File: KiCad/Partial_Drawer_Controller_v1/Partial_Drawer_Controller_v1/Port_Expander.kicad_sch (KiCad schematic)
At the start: 3 parts, among them U5 PCA9554PW,118

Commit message: feat: finishing first draft for `partial_drawer_controller_v1` schematic
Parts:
- removed C52: 100n_50V, Capacitor_SMD:C_0402_1005Metric, symbol _C_0402:100n_50V
- removed R220: 10K, Resistor_SMD:R_0402_1005Metric, symbol _R_0402:10K
- removed U5: PCA9554PW,118, Package_SO:TSSOP-16_4.4x5mm_P0.65mm, symbol _Interface_Expansion:PCA9554PW,118
- added C72: 100n_50V, Capacitor_SMD:C_0402_1005Metric, symbol _C_0402:100n_50V
- added R241: 10K, Resistor_SMD:R_0402_1005Metric, symbol _R_0402:10K
- added U5: PCA9535PW,118, Package_SO:TSSOP-24_4.4x7.8mm_P0.65mm, symbol _Interface_Expansion:PCA9535PW,118
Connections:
- net +5V: now also C72.1, R241.1, U5.24 (VDD)
- net A0: now also U5.21 (A0)
- net A1: now also U5.2 (A1)
- net A2: now also U5.3 (A2)
- net GND: now also C72.2, U5.12 (VSS)
- net SCL: now also U5.23 (SDA)
- net SDA: now also U5.22 (SCL)
- net ~INT: now also R241.2, U5.1 (~INT)
- new net IO0_0: U5.4 (IO0_0)
- new net IO0_1: U5.5 (IO0_1)
- new net IO0_2: U5.6 (IO0_2)
- new net IO0_3: U5.7 (IO0_3)
- new net IO0_4: U5.8 (IO0_4)
- new net IO0_5: U5.9 (IO0_5)
- new net IO0_6: U5.10 (IO0_6)
- new net IO0_7: U5.11 (IO0_7)
- new net IO1_0: U5.13 (IO1_0)
- new net IO1_1: U5.14 (IO1_1)
- new net IO1_2: U5.15 (IO1_2)
- new net IO1_3: U5.16 (IO1_3)
- new net IO1_4: U5.17 (IO1_4)
- new net IO1_5: U5.18 (IO1_5)
- new net IO1_6: U5.19 (IO1_6)
- new net IO1_7: U5.20 (IO1_7)

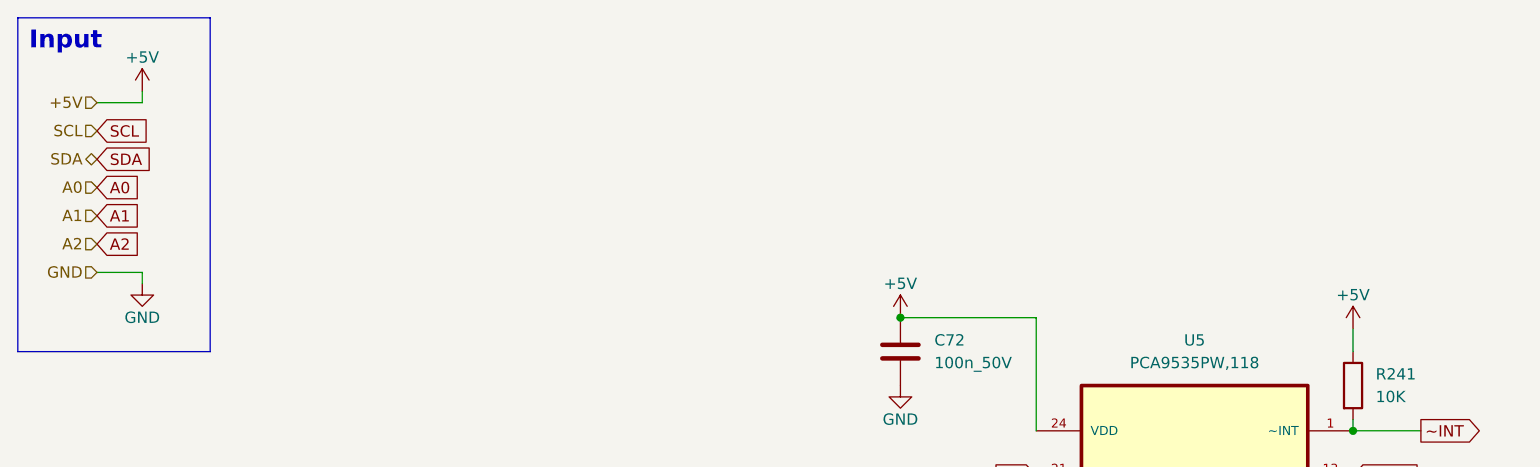
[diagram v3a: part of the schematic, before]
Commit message: feat: routing almost done - design rule check still missing
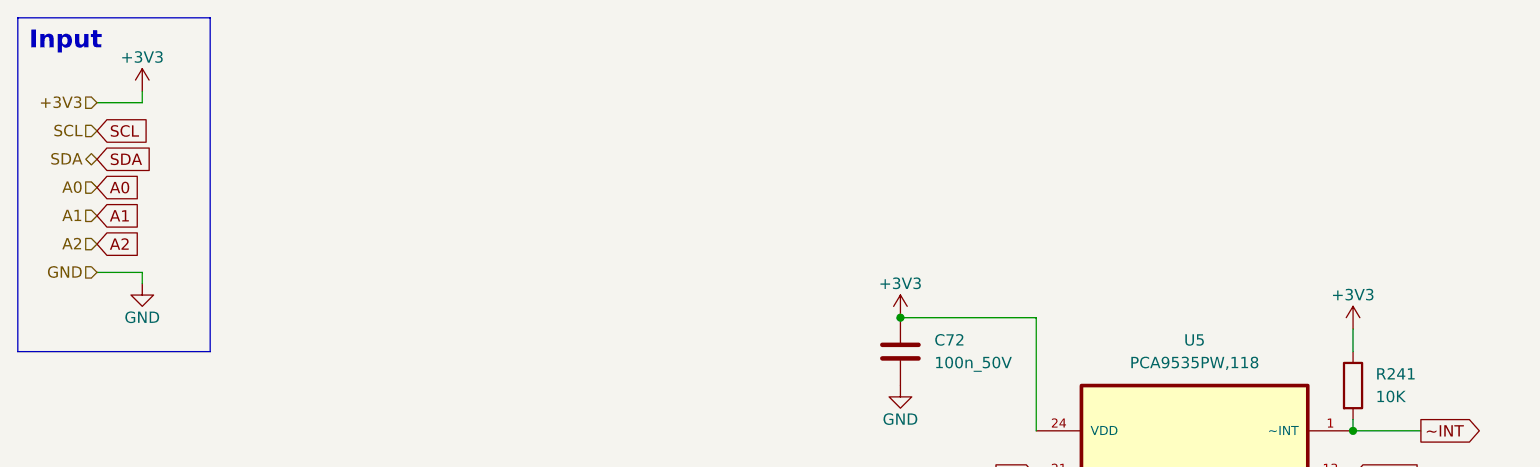
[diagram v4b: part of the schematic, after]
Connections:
- net +5V renamed +3V3
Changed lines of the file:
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@@
 		)
 	)
-	(hierarchical_label "+5V"
+	(hierarchical_label "+3V3"
 		(shape input)
 		(at 24.13 25.4 180)
@@
 			)
 			(justify left)
+		)
+	)
+	(symbol
+		(lib_id "power:+3V3")
+		(at 114.3 49.53 0)
+		(unit 1)
+		(exclude_from_sim no)
+		(in_bom yes)
+		(on_board yes)
+		(dnp no)
+		(property "Reference" "#PWR0192"
+			(at 114.3 53.34 0)
+			(effects
+				(font
+					(size 1.27 1.27)
+				)
+				(hide yes)
+			)
+		)
+		(property "Value" "+3V3"
+			(at 114.3 45.72 0)
+			(effects
+				(font
+					(size 1.27 1.27)
+				)
+			)
+		)
+		(property "Footprint" ""
+			(at 114.3 49.53 0)
+			(effects
+				(font
+					(size 1.27 1.27)
+				)
+				(hide yes)
+			)
+		)
+		(property "Datasheet" ""
+			(at 114.3 49.53 0)
+			(effects
+				(font
+					(size 1.27 1.27)
+				)
+				(hide yes)
+			)
+		)
+		(property "Description" ""
+			(at 114.3 49.53 0)
+			(effects
+				(font
+					(size 1.27 1.27)
+				)
+				(hide yes)
+			)
+		)
+		(pin "1"
+		)
+		(instances
+			(project "Partial_Drawer_Controller_v1"
+				(path "/57f8c193-fe09-43d3-9441-dbd40881d2aa/d19b84cd-4ee4-4d95-811d-38c072072447/1435e788-24b0-4d35-b04b-da1d0e65b7d1"
+					(reference "#PWR0192")
+					(unit 1)
+				)
+				(path "/57f8c193-fe09-43d3-9441-dbd40881d2aa/d19b84cd-4ee4-4d95-811d-38c072072447/336007e7-e816-41c4-9905-48078505cd87"
+					(reference "#PWR0196")
+					(unit 1)
+				)
+				(path "/57f8c193-fe09-43d3-9441-dbd40881d2aa/d19b84cd-4ee4-4d95-811d-38c072072447/784b2884-d726-456d-9cf9-7365a865d845"
+					(reference "#PWR0200")
+					(unit 1)
+				)
+			)
 		)
 	)
@@
 	)
 	(symbol
-		(lib_id "power:+5V")
-		(at 165.1 50.8 0)
-		(unit 1)
-		(exclude_from_sim no)
-		(in_bom yes)
-		(on_board yes)
-		(dnp no)
-		(property "Reference" "#PWR0300"
-			(at 165.1 54.61 0)
-			(effects
-				(font
-					(size 1.27 1.27)
-				)
-				(hide yes)
-			)
-		)
-		(property "Value" "+5V"
-			(at 165.1 46.99 0)
-			(effects
-				(font
-					(size 1.27 1.27)
-				)
-			)
-		)
-		(property "Footprint" ""
-			(at 165.1 50.8 0)
-			(effects
-				(font
-					(size 1.27 1.27)
-				)
-				(hide yes)
-			)
-		)
-		(property "Datasheet" ""
-			(at 165.1 50.8 0)
-			(effects
-				(font
-					(size 1.27 1.27)
-				)
-				(hide yes)
-			)
-		)
-		(property "Description" ""
-			(at 165.1 50.8 0)
-			(effects
-				(font
-					(size 1.27 1.27)
-				)
-				(hide yes)
-			)
-		)
-		(pin "1"
-		)
-		(instances
-			(project "Partial_Drawer_Controller_v1"
-				(path "/57f8c193-fe09-43d3-9441-dbd40881d2aa/d19b84cd-4ee4-4d95-811d-38c072072447/784b2884-d726-456d-9cf9-7365a865d845"
-					(reference "#PWR0300")
-					(unit 1)
-				)
-				(path "/57f8c193-fe09-43d3-9441-dbd40881d2aa/d19b84cd-4ee4-4d95-811d-38c072072447/1435e788-24b0-4d35-b04b-da1d0e65b7d1"
-					(reference "#PWR0195")
-					(unit 1)
-				)
-				(path "/57f8c193-fe09-43d3-9441-dbd40881d2aa/d19b84cd-4ee4-4d95-811d-38c072072447/336007e7-e816-41c4-9905-48078505cd87"
-					(reference "#PWR0203")
-					(unit 1)
-				)
-			)
-		)
-	)
-	(symbol
 		(lib_id "_C_0402:100n_50V")
 		(at 114.3 53.34 0)
@@
 				(path "/57f8c193-fe09-43d3-9441-dbd40881d2aa/d19b84cd-4ee4-4d95-811d-38c072072447/336007e7-e816-41c4-9905-48078505cd87"
 					(reference "C53")
-					(unit 1)
-				)
-			)
-		)
-	)
-	(symbol
-		(lib_id "power:+5V")
-		(at 29.21 24.13 0)
-		(unit 1)
-		(exclude_from_sim no)
-		(in_bom yes)
-		(on_board yes)
-		(dnp no)
-		(property "Reference" "#PWR0182"
-			(at 29.21 27.94 0)
-			(effects
-				(font
-					(size 1.27 1.27)
-				)
-				(hide yes)
-			)
-		)
-		(property "Value" "+5V"
-			(at 29.21 20.32 0)
-			(effects
-				(font
-					(size 1.27 1.27)
-				)
-			)
-		)
-		(property "Footprint" ""
-			(at 29.21 24.13 0)
-			(effects
-				(font
-					(size 1.27 1.27)
-				)
-				(hide yes)
-			)
-		)
-		(property "Datasheet" ""
-			(at 29.21 24.13 0)
-			(effects
-				(font
-					(size 1.27 1.27)
-				)
-				(hide yes)
-			)
-		)
-		(property "Description" ""
-			(at 29.21 24.13 0)
-			(effects
-				(font
-					(size 1.27 1.27)
-				)
-				(hide yes)
-			)
-		)
-		(pin "1"
-		)
-		(instances
-			(project "Partial_Drawer_Controller_v1"
-				(path "/57f8c193-fe09-43d3-9441-dbd40881d2aa/d19b84cd-4ee4-4d95-811d-38c072072447/784b2884-d726-456d-9cf9-7365a865d845"
-					(reference "#PWR0182")
-					(unit 1)
-				)
-				(path "/57f8c193-fe09-43d3-9441-dbd40881d2aa/d19b84cd-4ee4-4d95-811d-38c072072447/1435e788-24b0-4d35-b04b-da1d0e65b7d1"
-					(reference "#PWR0186")
-					(unit 1)
-				)
-				(path "/57f8c193-fe09-43d3-9441-dbd40881d2aa/d19b84cd-4ee4-4d95-811d-38c072072447/336007e7-e816-41c4-9905-48078505cd87"
-					(reference "#PWR0198")
 					(unit 1)
 				)
@@
 	)
 	(symbol
-		(lib_id "power:+5V")
-		(at 114.3 49.53 0)
+		(lib_id "power:+3V3")
+		(at 29.21 24.13 0)
 		(unit 1)
 		(exclude_from_sim no)
@@
 		(on_board yes)
 		(dnp no)
-		(property "Reference" "#PWR0292"
-			(at 114.3 53.34 0)
-			(effects
-				(font
-					(size 1.27 1.27)
-				)
-				(hide yes)
-			)
-		)
-		(property "Value" "+5V"
-			(at 114.3 45.72 0)
+		(property "Reference" "#PWR0182"
+			(at 29.21 27.94 0)
+			(effects
+				(font
+					(size 1.27 1.27)
+				)
+				(hide yes)
+			)
+		)
+		(property "Value" "+3V3"
+			(at 29.21 20.32 0)
 			(effects
 				(font
@@
 		)
 		(property "Footprint" ""
-			(at 114.3 49.53 0)
+			(at 29.21 24.13 0)
 			(effects
 				(font
@@
 		)
 		(property "Datasheet" ""
-			(at 114.3 49.53 0)
+			(at 29.21 24.13 0)
 			(effects
 				(font
@@
 		)
 		(property "Description" ""
-			(at 114.3 49.53 0)
+			(at 29.21 24.13 0)
 			(effects
 				(font
@@
 		(instances
 			(project "Partial_Drawer_Controller_v1"
+				(path "/57f8c193-fe09-43d3-9441-dbd40881d2aa/d19b84cd-4ee4-4d95-811d-38c072072447/1435e788-24b0-4d35-b04b-da1d0e65b7d1"
+					(reference "#PWR0182")
+					(unit 1)
+				)
+				(path "/57f8c193-fe09-43d3-9441-dbd40881d2aa/d19b84cd-4ee4-4d95-811d-38c072072447/336007e7-e816-41c4-9905-48078505cd87"
+					(reference "#PWR0186")
+					(unit 1)
+				)
 				(path "/57f8c193-fe09-43d3-9441-dbd40881d2aa/d19b84cd-4ee4-4d95-811d-38c072072447/784b2884-d726-456d-9cf9-7365a865d845"
-					(reference "#PWR0292")
-					(unit 1)
-				)
+					(reference "#PWR0198")
+					(unit 1)
+				)
+			)
+		)
+	)
+	(symbol
+		(lib_id "power:+3V3")
+		(at 165.1 50.8 0)
+		(unit 1)
+		(exclude_from_sim no)
+		(in_bom yes)
+		(on_board yes)
+		(dnp no)
+		(property "Reference" "#PWR0195"
+			(at 165.1 54.61 0)
+			(effects
+				(font
+					(size 1.27 1.27)
+				)
+				(hide yes)
+			)
+		)
+		(property "Value" "+3V3"
+			(at 165.1 46.99 0)
+			(effects
+				(font
+					(size 1.27 1.27)
+				)
+			)
+		)
+		(property "Footprint" ""
+			(at 165.1 50.8 0)
+			(effects
+				(font
+					(size 1.27 1.27)
+				)
+				(hide yes)
+			)
+		)
+		(property "Datasheet" ""
+			(at 165.1 50.8 0)
+			(effects
+				(font
+					(size 1.27 1.27)
+				)
+				(hide yes)
+			)
+		)
+		(property "Description" ""
+			(at 165.1 50.8 0)
+			(effects
+				(font
+					(size 1.27 1.27)
+				)
+				(hide yes)
+			)
+		)
+		(pin "1"
+		)
+		(instances
+			(project "Partial_Drawer_Controller_v1"
 				(path "/57f8c193-fe09-43d3-9441-dbd40881d2aa/d19b84cd-4ee4-4d95-811d-38c072072447/1435e788-24b0-4d35-b04b-da1d0e65b7d1"
-					(reference "#PWR0192")
+					(reference "#PWR0195")
 					(unit 1)
 				)
 				(path "/57f8c193-fe09-43d3-9441-dbd40881d2aa/d19b84cd-4ee4-4d95-811d-38c072072447/336007e7-e816-41c4-9905-48078505cd87"
-					(reference "#PWR0200")
-					(unit 1)
-				)
+					(reference "#PWR0203")
+					(unit 1)
+				)
+				(path "/57f8c193-fe09-43d3-9441-dbd40881d2aa/d19b84cd-4ee4-4d95-811d-38c072072447/784b2884-d726-456d-9cf9-7365a865d845"
+					(reference "#PWR0204")
+					(unit 1)
+				)

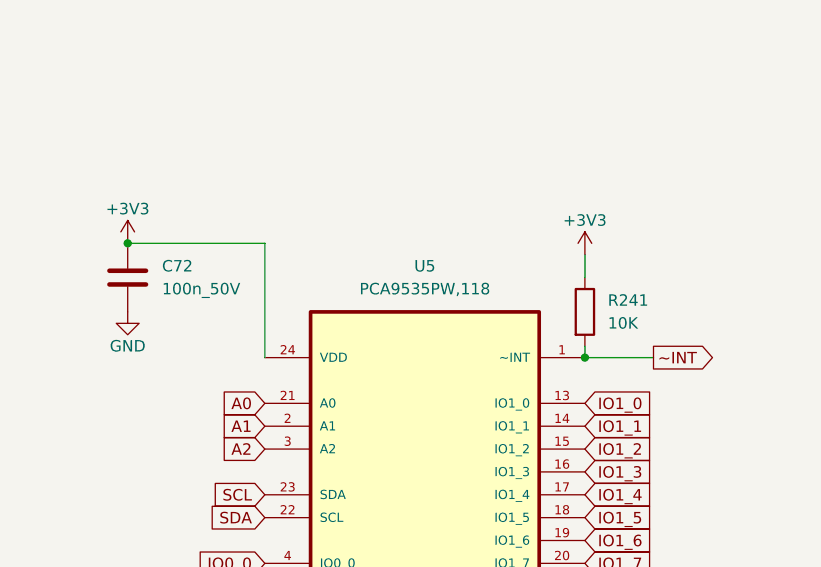
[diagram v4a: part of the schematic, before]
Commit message: feat: minor adjustments and new export of manufacturing files for `Partial_Drawer_controller_v1`
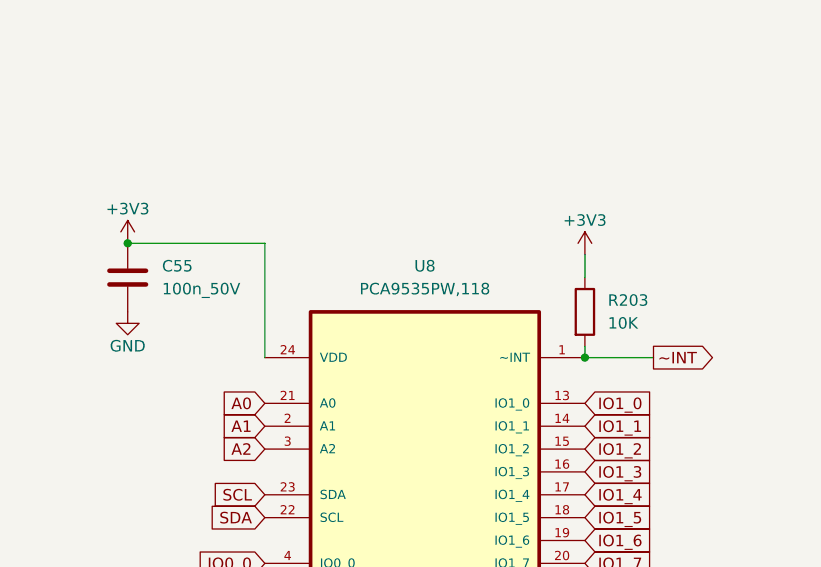
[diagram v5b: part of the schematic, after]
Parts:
- renumbered C72 to C55, R241 to R203, U5 to U8
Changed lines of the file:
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@@
 		(on_board yes)
 		(dnp no)
-		(property "Reference" "#PWR0192"
+		(property "Reference" "#PWR0218"
 			(at 114.3 53.34 0)
 			(effects
@@
 			(project "Partial_Drawer_Controller_v1"
 				(path "/57f8c193-fe09-43d3-9441-dbd40881d2aa/d19b84cd-4ee4-4d95-811d-38c072072447/1435e788-24b0-4d35-b04b-da1d0e65b7d1"
-					(reference "#PWR0192")
+					(reference "#PWR0218")
 					(unit 1)
 				)
 				(path "/57f8c193-fe09-43d3-9441-dbd40881d2aa/d19b84cd-4ee4-4d95-811d-38c072072447/336007e7-e816-41c4-9905-48078505cd87"
-					(reference "#PWR0196")
+					(reference "#PWR0224")
 					(unit 1)
 				)
 				(path "/57f8c193-fe09-43d3-9441-dbd40881d2aa/d19b84cd-4ee4-4d95-811d-38c072072447/784b2884-d726-456d-9cf9-7365a865d845"
-					(reference "#PWR0200")
+					(reference "#PWR0230")
 					(unit 1)
 				)
@@
 		(on_board yes)
 		(dnp no)
-		(property "Reference" "#PWR0293"
+		(property "Reference" "#PWR0231"
 			(at 114.3 63.5 0)
 			(effects
@@
 			(project "Partial_Drawer_Controller_v1"
 				(path "/57f8c193-fe09-43d3-9441-dbd40881d2aa/d19b84cd-4ee4-4d95-811d-38c072072447/784b2884-d726-456d-9cf9-7365a865d845"
-					(reference "#PWR0293")
+					(reference "#PWR0231")
 					(unit 1)
 				)
 				(path "/57f8c193-fe09-43d3-9441-dbd40881d2aa/d19b84cd-4ee4-4d95-811d-38c072072447/1435e788-24b0-4d35-b04b-da1d0e65b7d1"
-					(reference "#PWR0193")
+					(reference "#PWR0219")
 					(unit 1)
 				)
 				(path "/57f8c193-fe09-43d3-9441-dbd40881d2aa/d19b84cd-4ee4-4d95-811d-38c072072447/336007e7-e816-41c4-9905-48078505cd87"
-					(reference "#PWR0201")
+					(reference "#PWR0225")
 					(unit 1)
 				)
@@
 		(dnp no)
 		(fields_autoplaced yes)
-		(property "Reference" "U5"
+		(property "Reference" "U8"
 			(at 147.32 52.07 0)
 			(effects
@@
 			(project "Partial_Drawer_Controller_v1"
 				(path "/57f8c193-fe09-43d3-9441-dbd40881d2aa/d19b84cd-4ee4-4d95-811d-38c072072447/1435e788-24b0-4d35-b04b-da1d0e65b7d1"
-					(reference "U5")
+					(reference "U8")
 					(unit 1)
 				)
@@
 				)
 				(path "/57f8c193-fe09-43d3-9441-dbd40881d2aa/d19b84cd-4ee4-4d95-811d-38c072072447/784b2884-d726-456d-9cf9-7365a865d845"
-					(reference "U19")
+					(reference "U10")
 					(unit 1)
 				)
@@
 		(dnp no)
 		(fields_autoplaced yes)
-		(property "Reference" "R241"
+		(property "Reference" "R203"
 			(at 167.64 55.8799 0)
 			(effects
@@
 			(project "Partial_Drawer_Controller_v1"
 				(path "/57f8c193-fe09-43d3-9441-dbd40881d2aa/d19b84cd-4ee4-4d95-811d-38c072072447/784b2884-d726-456d-9cf9-7365a865d845"
-					(reference "R241")
+					(reference "R203")
 					(unit 1)
 				)
 				(path "/57f8c193-fe09-43d3-9441-dbd40881d2aa/d19b84cd-4ee4-4d95-811d-38c072072447/1435e788-24b0-4d35-b04b-da1d0e65b7d1"
-					(reference "R220")
+					(reference "R201")
 					(unit 1)
 				)
 				(path "/57f8c193-fe09-43d3-9441-dbd40881d2aa/d19b84cd-4ee4-4d95-811d-38c072072447/336007e7-e816-41c4-9905-48078505cd87"
-					(reference "R223")
+					(reference "R202")
 					(unit 1)
 				)
@@
 		(dnp no)
 		(fields_autoplaced yes)
-		(property "Reference" "C72"
+		(property "Reference" "C55"
 			(at 118.11 52.0699 0)
 			(effects
@@
 			(project "Partial_Drawer_Controller_v1"
 				(path "/57f8c193-fe09-43d3-9441-dbd40881d2aa/d19b84cd-4ee4-4d95-811d-38c072072447/784b2884-d726-456d-9cf9-7365a865d845"
-					(reference "C72")
+					(reference "C55")
 					(unit 1)
 				)
 				(path "/57f8c193-fe09-43d3-9441-dbd40881d2aa/d19b84cd-4ee4-4d95-811d-38c072072447/1435e788-24b0-4d35-b04b-da1d0e65b7d1"
-					(reference "C52")
+					(reference "C53")
 					(unit 1)
 				)
 				(path "/57f8c193-fe09-43d3-9441-dbd40881d2aa/d19b84cd-4ee4-4d95-811d-38c072072447/336007e7-e816-41c4-9905-48078505cd87"
-					(reference "C53")
+					(reference "C54")
 					(unit 1)
 				)
@@
 		(on_board yes)
 		(dnp no)
-		(property "Reference" "#PWR0183"
+		(property "Reference" "#PWR0229"
 			(at 29.21 52.07 0)
 			(effects
@@
 			(project "Partial_Drawer_Controller_v1"
 				(path "/57f8c193-fe09-43d3-9441-dbd40881d2aa/d19b84cd-4ee4-4d95-811d-38c072072447/784b2884-d726-456d-9cf9-7365a865d845"
-					(reference "#PWR0183")
+					(reference "#PWR0229")
 					(unit 1)
 				)
 				(path "/57f8c193-fe09-43d3-9441-dbd40881d2aa/d19b84cd-4ee4-4d95-811d-38c072072447/1435e788-24b0-4d35-b04b-da1d0e65b7d1"
-					(reference "#PWR0187")
+					(reference "#PWR0217")
 					(unit 1)
 				)
 				(path "/57f8c193-fe09-43d3-9441-dbd40881d2aa/d19b84cd-4ee4-4d95-811d-38c072072447/336007e7-e816-41c4-9905-48078505cd87"
-					(reference "#PWR0199")
+					(reference "#PWR0223")
 					(unit 1)
 				)
@@
 		(on_board yes)
 		(dnp no)
-		(property "Reference" "#PWR0182"
+		(property "Reference" "#PWR0216"
 			(at 29.21 27.94 0)
 			(effects
@@
 			(project "Partial_Drawer_Controller_v1"
 				(path "/57f8c193-fe09-43d3-9441-dbd40881d2aa/d19b84cd-4ee4-4d95-811d-38c072072447/1435e788-24b0-4d35-b04b-da1d0e65b7d1"
-					(reference "#PWR0182")
+					(reference "#PWR0216")
 					(unit 1)
 				)
 				(path "/57f8c193-fe09-43d3-9441-dbd40881d2aa/d19b84cd-4ee4-4d95-811d-38c072072447/336007e7-e816-41c4-9905-48078505cd87"
-					(reference "#PWR0186")
+					(reference "#PWR0222")
 					(unit 1)
 				)
 				(path "/57f8c193-fe09-43d3-9441-dbd40881d2aa/d19b84cd-4ee4-4d95-811d-38c072072447/784b2884-d726-456d-9cf9-7365a865d845"
-					(reference "#PWR0198")
+					(reference "#PWR0228")
 					(unit 1)
 				)
@@
 		(on_board yes)
 		(dnp no)
-		(property "Reference" "#PWR0195"
+		(property "Reference" "#PWR0221"
 			(at 165.1 54.61 0)
 			(effects
@@
 			(project "Partial_Drawer_Controller_v1"
 				(path "/57f8c193-fe09-43d3-9441-dbd40881d2aa/d19b84cd-4ee4-4d95-811d-38c072072447/1435e788-24b0-4d35-b04b-da1d0e65b7d1"
-					(reference "#PWR0195")
+					(reference "#PWR0221")
 					(unit 1)
 				)
 				(path "/57f8c193-fe09-43d3-9441-dbd40881d2aa/d19b84cd-4ee4-4d95-811d-38c072072447/336007e7-e816-41c4-9905-48078505cd87"
-					(reference "#PWR0203")
+					(reference "#PWR0227")
 					(unit 1)
 				)
 				(path "/57f8c193-fe09-43d3-9441-dbd40881d2aa/d19b84cd-4ee4-4d95-811d-38c072072447/784b2884-d726-456d-9cf9-7365a865d845"
-					(reference "#PWR0204")
+					(reference "#PWR0233")
 					(unit 1)
 				)
@@
 		(on_board yes)
 		(dnp no)
-		(property "Reference" "#PWR0285"
+		(property "Reference" "#PWR0232"
 			(at 127 116.84 0)
 			(effects
@@
 			(project "Partial_Drawer_Controller_v1"
 				(path "/57f8c193-fe09-43d3-9441-dbd40881d2aa/d19b84cd-4ee4-4d95-811d-38c072072447/784b2884-d726-456d-9cf9-7365a865d845"
-					(reference "#PWR0285")
+					(reference "#PWR0232")
 					(unit 1)
 				)
 				(path "/57f8c193-fe09-43d3-9441-dbd40881d2aa/d19b84cd-4ee4-4d95-811d-38c072072447/1435e788-24b0-4d35-b04b-da1d0e65b7d1"
-					(reference "#PWR0194")
+					(reference "#PWR0220")
 					(unit 1)
 				)
 				(path "/57f8c193-fe09-43d3-9441-dbd40881d2aa/d19b84cd-4ee4-4d95-811d-38c072072447/336007e7-e816-41c4-9905-48078505cd87"
-					(reference "#PWR0202")
-					(unit 1)
-				)
+					(reference "#PWR0226")
+					(unit 1)
+				)
